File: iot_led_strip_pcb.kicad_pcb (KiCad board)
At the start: 2 copper layers, 80 x 50 mm, 79 parts, among them J1 GT-USB-7010ASV, J2 12V PWR, J3 5V PWR, J4 LED 5050, J5 I2C Expansion, J7 NEOPIXEL, Q1 S8050_C105433, Q2 S8050_C105433, Q3 UMW30N06, Q4 UMW30N06, Q5 UMW30N06, SW1 RESET, SW2 FLASH, U1 CH340G, U3 ESP-12E, U4 AMS1117-5.0, U5 AMS1117-3.3, U6 MCP1416, U7 MCP1416, U8 MCP1416, Y1 Crystal_12MHz

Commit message: initial layout rev 0.1
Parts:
- moved TP6 3.30 mm to (68.2, 101.8)
- moved U4 1.60 mm to (74.3, 100.3)
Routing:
- net Earth: track 104.8 -> 109.3 mm, vias 20 -> 22
- net VDD_5V: track 177.0 -> 174.5 mm, vias 5 -> 7
- net /12VDC: track 100.2 -> 101.8 mm
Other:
- board text added: "+12V"
- board text added: "+3V3"
- board text added: "12V"
- board text added: "5V"
- board text added: "B"
- board text added: "Din"
- board text added: "G"
- board text added: "GND"
- board text added: "IoT LED Strip Driver"
- board text added: "R"
- board text added: "SCL"
- board text added: "SDA"

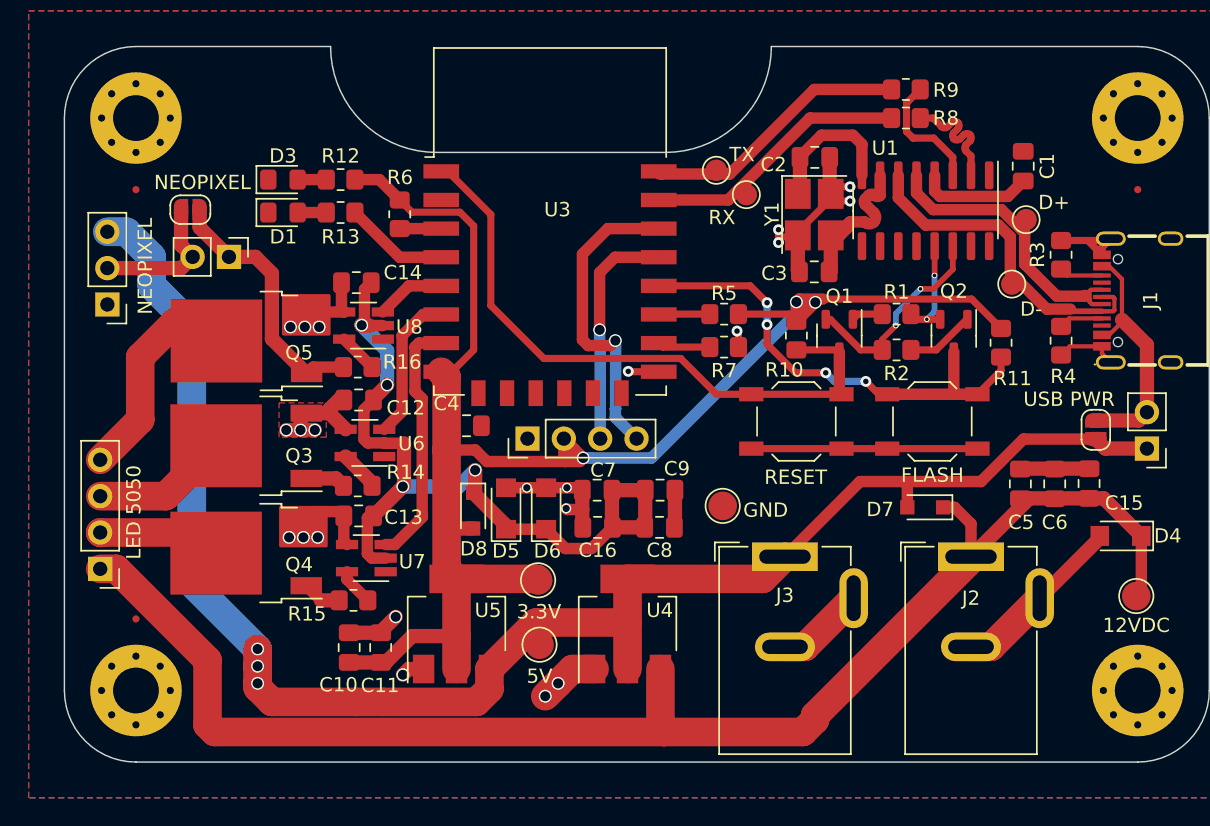
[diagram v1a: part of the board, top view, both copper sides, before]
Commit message: replaced all vias, reworked traces, DRC passes now
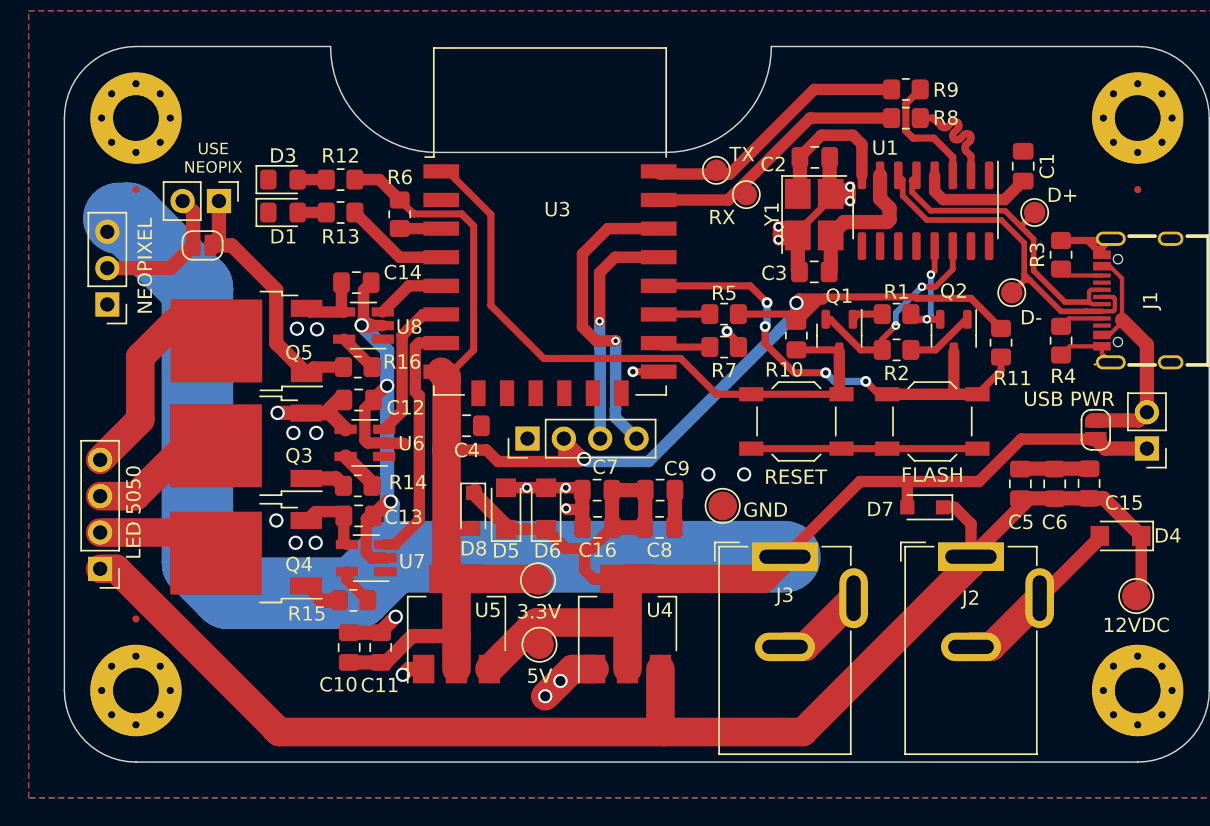
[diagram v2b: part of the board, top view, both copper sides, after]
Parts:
- moved JP4 3.96 mm to (45.8, 70.8)
- moved JP3 2.64 mm to (44.6, 73.9)
- moved TP1 0.78 mm to (102.8, 71.6)
- moved TP2 0.60 mm to (101.2, 77.2)
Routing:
- net VDD_5V: track 174.5 -> 196.6 mm, vias 7 -> 3
- net Net-(C1-Pad2): track 15.7 -> 9.09 mm
- net /GPIO0: track 36.4 -> 33.6 mm
- net /12VDC: track 101.8 -> 99.2 mm
- net /USB_to_Serial/USB_D+: track 19.9 -> 22.1 mm
- net Earth: track 109.3 -> 111.2 mm, vias 22 -> 23
- net /USB_to_Serial/USB_D-: track 23.2 -> 24.9 mm
- net /LED_driver/LED_R_GND: track 10.4 -> 9.56 mm
- net /SCL: track 22.2 -> 21.4 mm
- net +3.3V: track 117.2 -> 117.5 mm, vias 3 -> 2
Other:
- board text added: "USE NEOPIX"

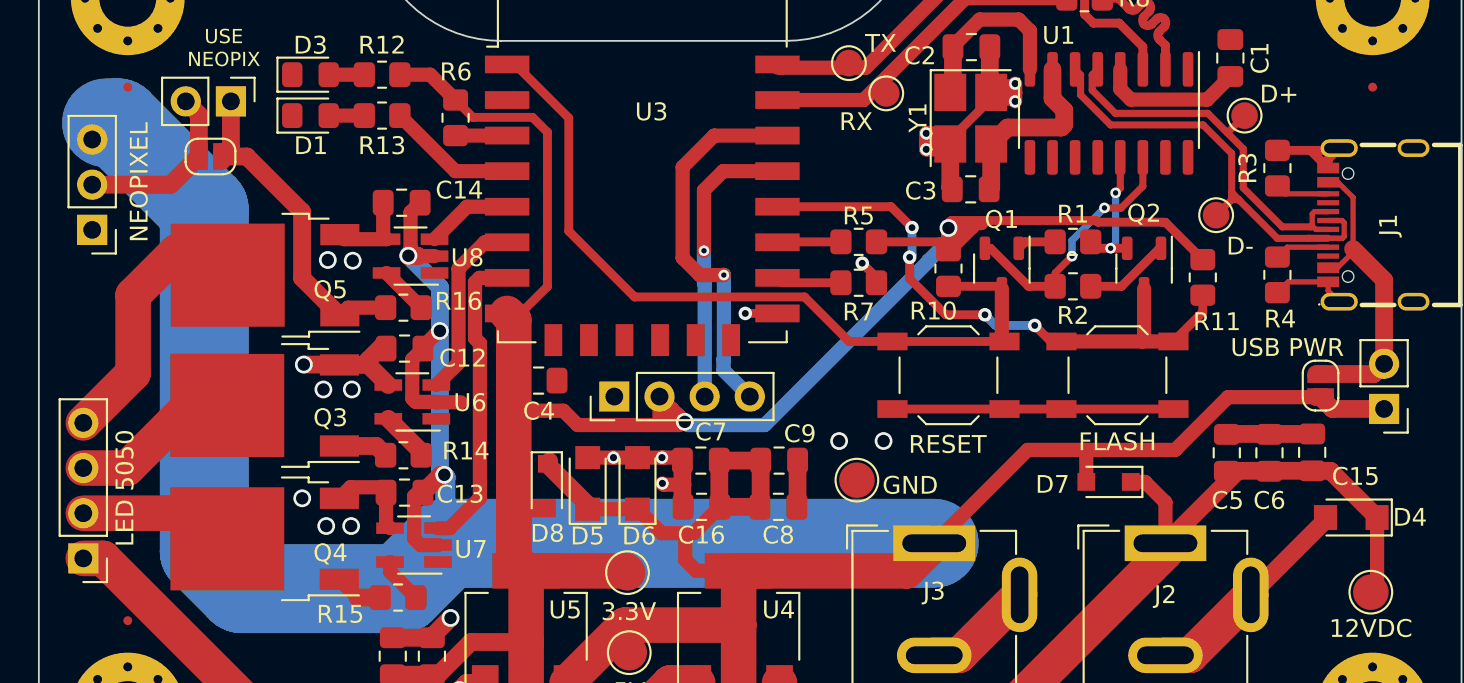
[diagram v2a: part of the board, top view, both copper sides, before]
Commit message: upgrade to kicad 7, some changes to pcb text
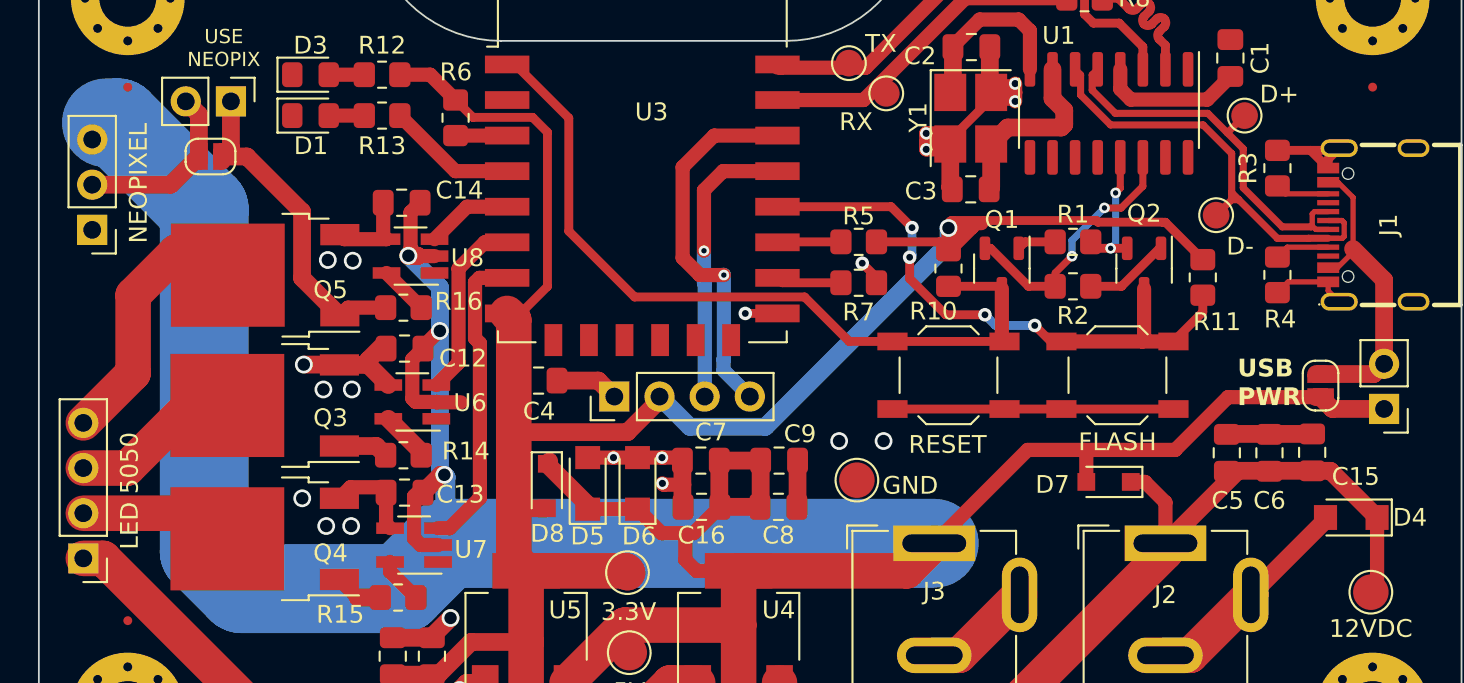
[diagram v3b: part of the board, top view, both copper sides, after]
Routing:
- net +3.3V: track 117.5 -> 113.5 mm, vias 2 -> 1
- net Earth: track 111.2 -> 114.8 mm
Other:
- board text added: "USB PWR"

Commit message: updated text, finalizing of board design, updated schematic rev number
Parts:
- added G***: LOGO, LOGO, B.Cu at (98.7, 77.8)
- moved FID1 70.0 mm to (110.0, 100.0)
- moved TP5 1.32 mm to (110.1, 97.1)
- moved J7 0.53 mm to (37.5, 78.2)
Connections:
- C12 pad 1: VDD_5V -> +5V
- C13 pad 1: VDD_5V -> +5V
- C14 pad 1: VDD_5V -> +5V
- C16 pad 1: VDD_5V -> +5V
- C7 pad 1: VDD_5V -> +5V
- C8 pad 1: VDD_5V -> +5V
- C9 pad 1: VDD_5V -> +5V
- D5 pad 1: VDD_5V -> +5V
- D6 pad 1: VDD_5V -> +5V
- D7 pad 2: VDD_5V -> +5V
- D8 pad 1: VDD_5V -> +5V
- J3 pad 1: VDD_5V -> +5V
- J7 pad 1: Earth -> +5V
- J7 pad 3: VDD_5V -> Earth
- JP1 pad 1: VDD_5V -> +5V
- JP2 pad 1: VDD_5V -> +5V
- TP6 pad 1: VDD_5V -> +5V
- U4 pad 2: VDD_5V -> +5V
- U5 pad 3: VDD_5V -> +5V
- U6 pad 2: VDD_5V -> +5V
- U7 pad 2: VDD_5V -> +5V
- U8 pad 2: VDD_5V -> +5V
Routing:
- net +5V: track 0.00 -> 226.4 mm, vias 0 -> 11
- net VDD_5V: track 196.6 -> 0.00 mm, vias 3 -> 0
- net Earth: track 114.8 -> 148.0 mm, vias 23 -> 28
- net /12VDC: track 99.2 -> 96.7 mm
- net /LED_driver/Din: track 10.1 -> 10.6 mm
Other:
- board text added: "0xjmux"
- board text added: "DBG"
- board text added: "PWR"
- board text added: "v1.0 - 08/2023"

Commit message: production files
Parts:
- removed U3: ESP-12E, RF_Module:ESP-12E
- added U2: ESP-12F, RF_Module:ESP-12E, F.Cu at (69.0, 72.2)

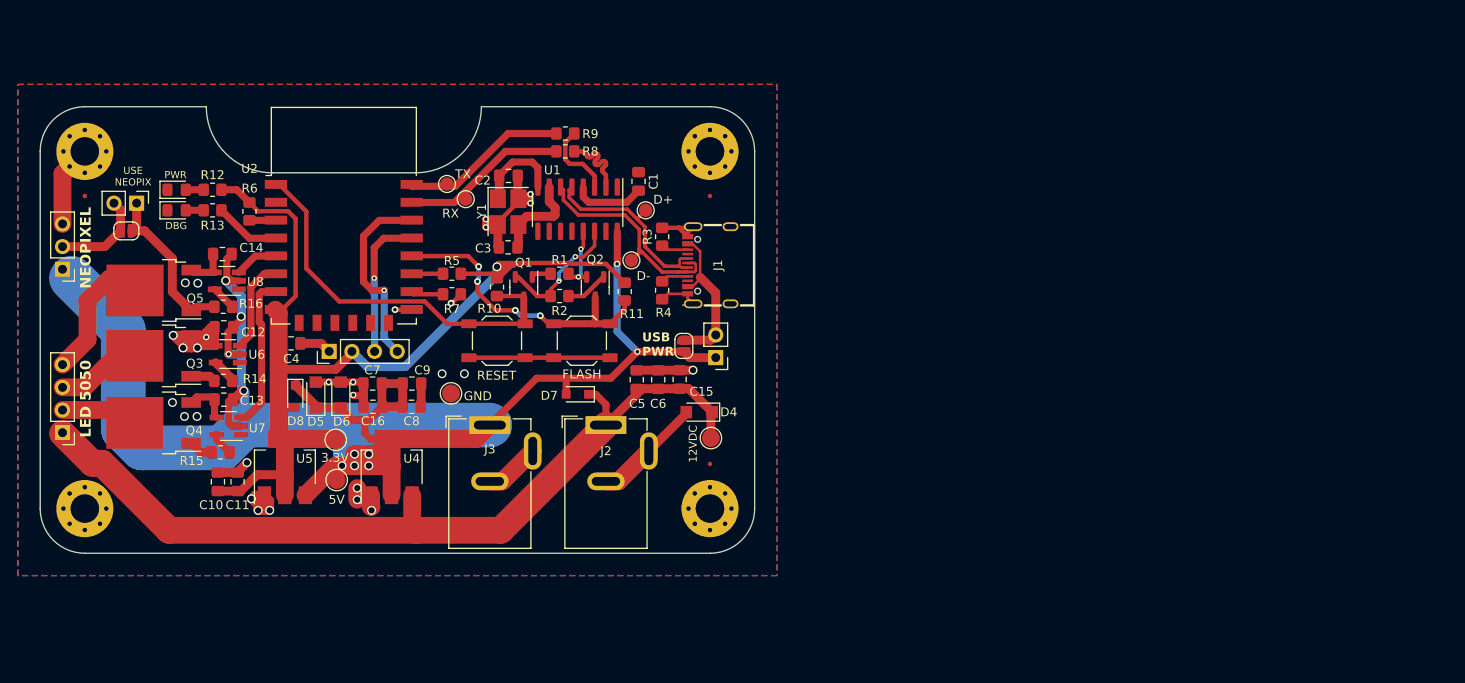
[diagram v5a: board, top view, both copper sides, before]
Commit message: some small changes to schematic, cleaned up old pcb
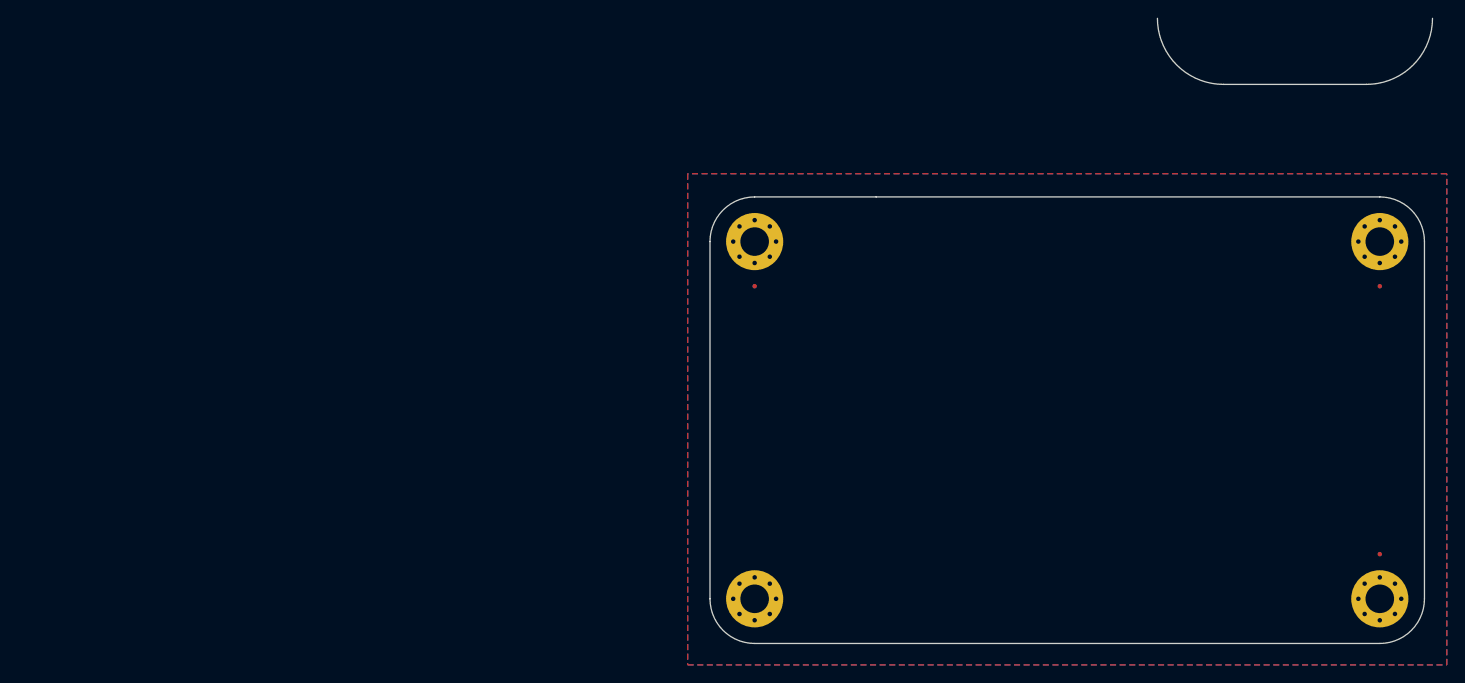
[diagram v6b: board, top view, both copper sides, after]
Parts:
- removed C1, C10, C7: 100nF, Capacitor_SMD:C_0805_2012Metric_Pad1.18x1.45mm_HandSolder
- removed C11, C12, C13, C14, C15, C16, C4, C5, C6, C8, C9: 10uF, Capacitor_SMD:C_0805_2012Metric_Pad1.18x1.45mm_HandSolder
- removed C2, C3: 22pF, Capacitor_SMD:C_0805_2012Metric_Pad1.18x1.45mm_HandSolder
- removed D1: LED, LED_SMD:LED_0805_2012Metric_Pad1.15x1.40mm_HandSolder
- removed D3: PWR_LED, LED_SMD:LED_0805_2012Metric_Pad1.15x1.40mm_HandSolder
- removed D4: SMF18A, Diode_SMD:D_SMF
- removed D5, D6: SMF5V0A, Diode_SMD:D_SMF
- removed D7, D8: 1N5819WS, Diode_SMD:D_SOD-323_HandSoldering
- removed G***: LOGO, LOGO
- removed J1: GT-USB-7010ASV, footprint:USB-C-SMD_G-SWITCH_GT-USB-7010ASV
- removed J2: 12V PWR, Connector_BarrelJack:BarrelJack_GCT_DCJ200-10-A_Horizontal
- removed J3: 5V PWR, Connector_BarrelJack:BarrelJack_GCT_DCJ200-10-A_Horizontal
- removed J4: LED 5050, Connector_PinHeader_2.54mm:PinHeader_1x04_P2.54mm_Vertical
- removed J5: I2C Expansion, Connector_PinHeader_2.54mm:PinHeader_1x04_P2.54mm_Vertical
- removed J7: NEOPIXEL, Connector_PinHeader_2.54mm:PinHeader_1x03_P2.54mm_Vertical
- removed JP1, JP4: Jumper_2_Bridged, Connector_PinHeader_2.54mm:PinHeader_1x02_P2.54mm_Vertical
- removed JP2: USB PWR, Jumper:SolderJumper-2_P1.3mm_Open_RoundedPad1.0x1.5mm
- removed JP3: NEOPIXEL, Jumper:SolderJumper-2_P1.3mm_Open_RoundedPad1.0x1.5mm
- removed Q1, Q2: S8050_C105433, Package_TO_SOT_SMD:SOT-23-3
- removed Q3, Q4, Q5: UMW30N06, Package_TO_SOT_SMD:TO-252-2
- removed R1, R10, R11, R2, R5, R6, R7: 10k, Resistor_SMD:R_0805_2012Metric_Pad1.20x1.40mm_HandSolder
- removed R12, R8, R9: 470, Resistor_SMD:R_0805_2012Metric_Pad1.20x1.40mm_HandSolder
- removed R13, R14, R15, R16: 100, Resistor_SMD:R_0805_2012Metric_Pad1.20x1.40mm_HandSolder
- removed R3, R4: 5.1k, Resistor_SMD:R_0805_2012Metric_Pad1.20x1.40mm_HandSolder
- removed SW1: RESET, Button_Switch_SMD:SW_SPST_TL3342
- removed SW2: FLASH, Button_Switch_SMD:SW_SPST_TL3342
- removed TP1: D+, TestPoint:TestPoint_Pad_D1.5mm
- removed TP2: D-, TestPoint:TestPoint_Pad_D1.5mm
- removed TP3: RX, TestPoint:TestPoint_Pad_D1.5mm
- removed TP4: TX, TestPoint:TestPoint_Pad_D1.5mm
- removed TP5: 12VDC, TestPoint:TestPoint_Pad_D2.0mm
- removed TP6: 5V, TestPoint:TestPoint_Pad_D2.0mm
- removed TP7: 3.3V, TestPoint:TestPoint_Pad_D2.0mm
- removed TP8: GND, TestPoint:TestPoint_Pad_D2.0mm
- removed U1: CH340G, Package_SO:SOIC-16_3.9x9.9mm_P1.27mm
- removed U2: ESP-12F, RF_Module:ESP-12E
- removed U4: AMS1117-5.0, Package_TO_SOT_SMD:SOT-223-3_TabPin2
- removed U5: AMS1117-3.3, Package_TO_SOT_SMD:SOT-223-3_TabPin2
- removed U6, U7, U8: MCP1416, Package_TO_SOT_SMD:SOT-23-5_HandSoldering
- removed Y1: Crystal_12MHz, Crystal:Crystal_SMD_3225-4Pin_3.2x2.5mm_HandSoldering
- moved FID1 75.7 mm to (185.0, 110.1)
- moved FID2 75.7 mm to (115.0, 80.1)
- moved FID3 75.7 mm to (185.0, 80.1)
- moved H1 75.7 mm to (115.0, 75.1)
- moved H2 75.7 mm to (185.0, 75.1)
- moved H3 75.7 mm to (115.0, 115.1)
- moved H4 75.7 mm to (185.0, 115.1)
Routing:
- net +5V: track 226.4 -> 0.00 mm, vias 11 -> 0
- net Earth: track 148.0 -> 0.00 mm, vias 28 -> 0
- net +3.3V: track 113.5 -> 0.00 mm, vias 1 -> 0
- net /12VDC: track 96.7 -> 0.00 mm
- net /~{RST}: track 44.2 -> 0.00 mm
- net /GPIO0: track 33.6 -> 0.00 mm, vias 4 -> 0
- net /USB_to_Serial/USB_D-: track 24.9 -> 0.00 mm
- net /USB_to_Serial/USB_D+: track 22.1 -> 0.00 mm
- net /SCL: track 21.4 -> 0.00 mm, vias 1 -> 0
- net /USB_to_Serial/TX: track 18.7 -> 0.00 mm
- net /USB_to_Serial/RX: track 18.6 -> 0.00 mm
- net Net-(JP3-A): track 18.6 -> 0.00 mm
- net VBUS: track 17.6 -> 0.00 mm
- net /LED_driver/LED_G: track 17.2 -> 0.00 mm
- net /SDA: track 16.2 -> 0.00 mm, vias 1 -> 0
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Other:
- board size 80 x 50 mm -> 80.9 x 70 mm
- board text removed: "+12V"
- board text removed: "+3V3"
- board text removed: "0xjmux"
- board text removed: "12V"
- board text removed: "5V"
- board text removed: "B"
- board text removed: "DBG"
- board text removed: "Din"
- board text removed: "G"
- board text removed: "GND"
- board text removed: "IoT LED Strip Driver"
- board text removed: "PWR"
- board text removed: "R"
- board text removed: "SCL"
- board text removed: "SDA"
- board text removed: "USB PWR"
- board text removed: "USE NEOPIX"
- board text removed: "v1.0 - 08/2023"
